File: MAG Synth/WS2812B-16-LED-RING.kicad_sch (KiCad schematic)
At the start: 33 parts

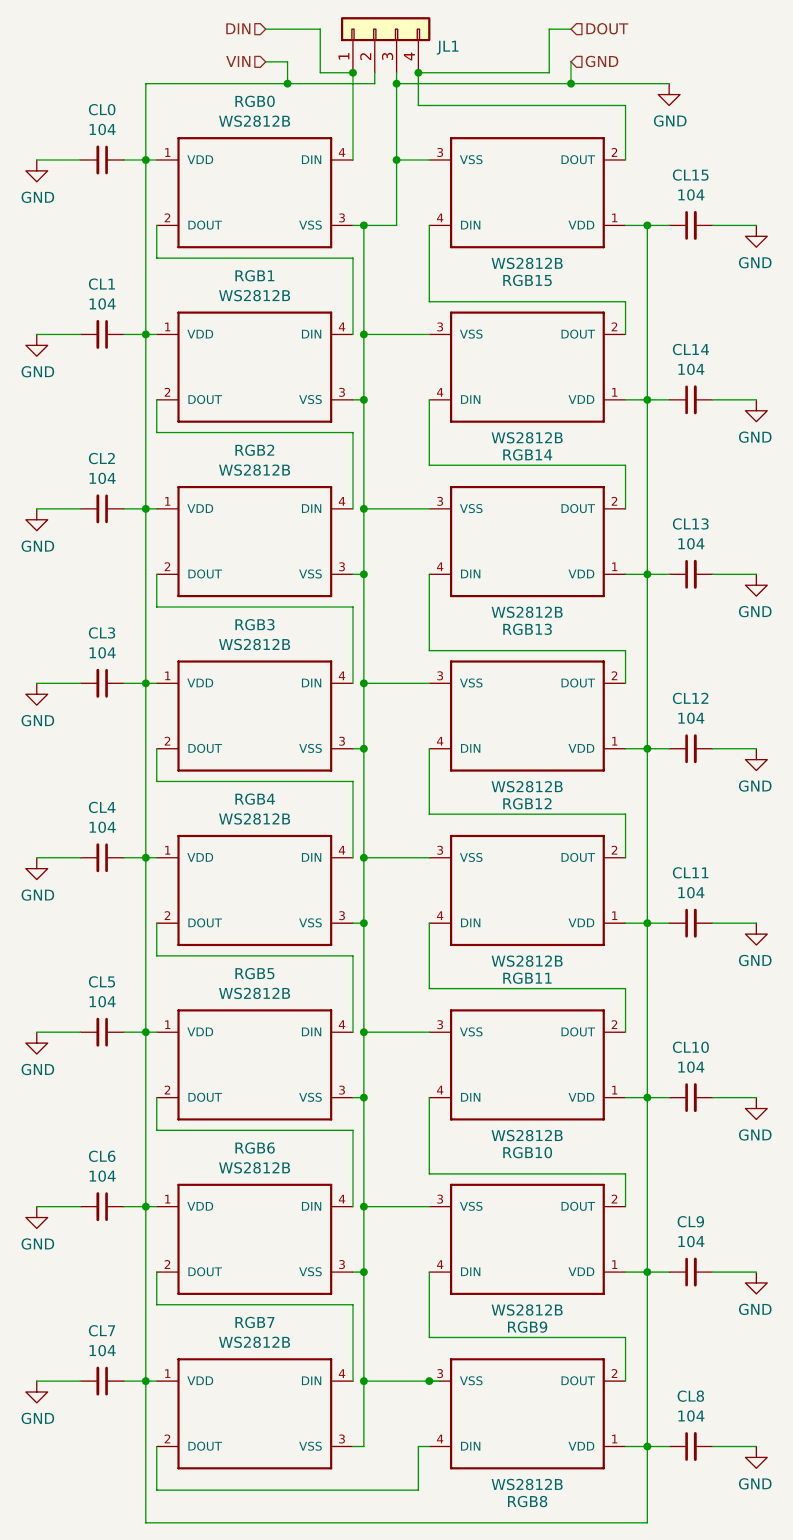
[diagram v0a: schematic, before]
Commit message: Schematic update
All ERC errors resolved.  100+ ERC warnings remain.
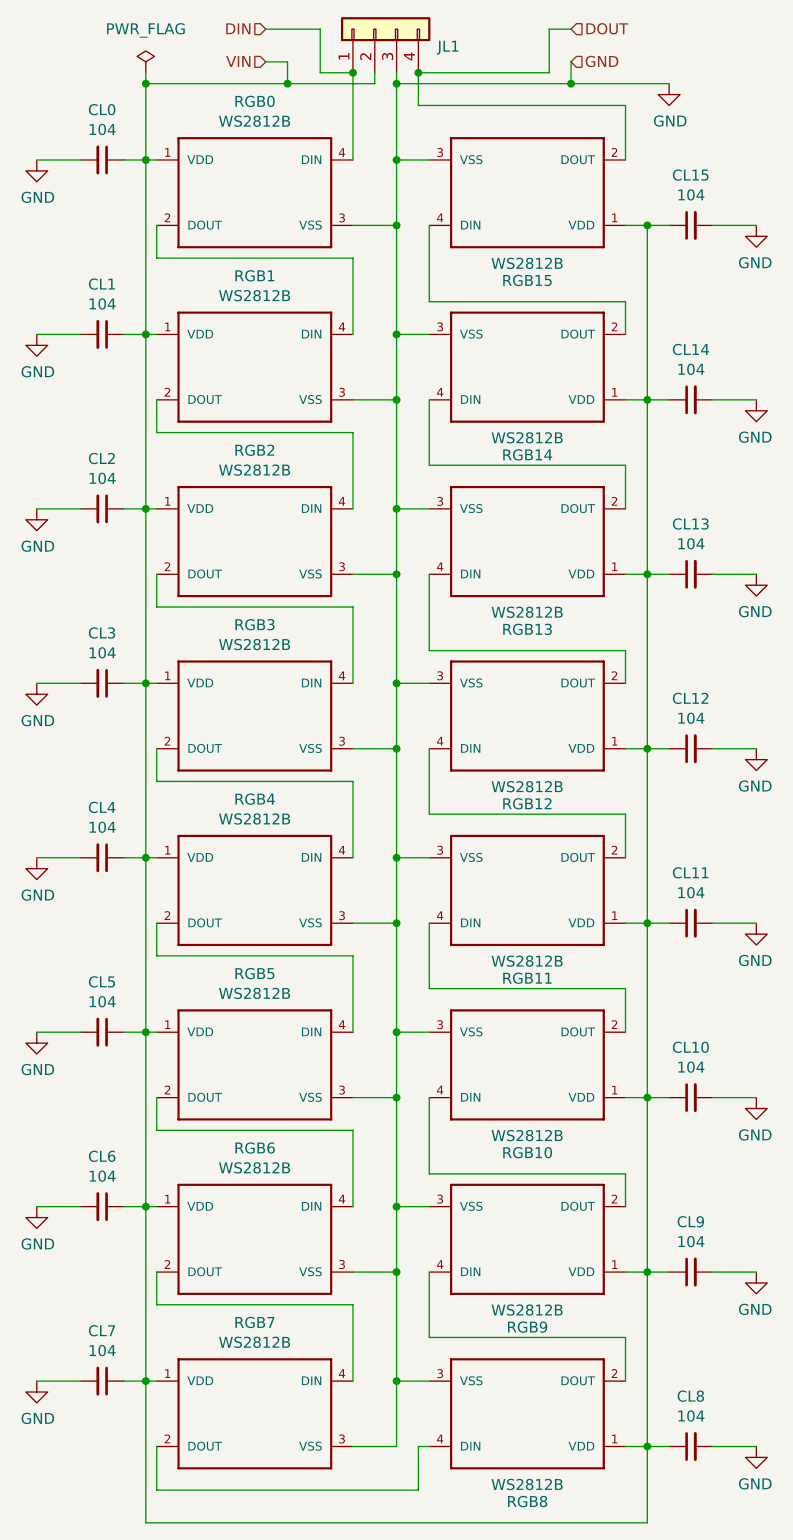
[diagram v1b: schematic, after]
